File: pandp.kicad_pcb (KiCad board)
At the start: 2 copper layers, 95 x 89 mm, 93 parts, among them IC1 ADP2303-5, P1 CONN_01X02, P10 CONN_01X04, P11 CONN_01X02, P12 CONN_02X04, P13 CONN_01X02, P14 CONN_01X04, P15 CONN_01X04, P16 CONN_01X03, P17 CONN_01X03, P18 CONN_01X03, P19 CONN_01X03, P2 CONN_01X03, P20 CONN_01X03, P21 CONN_01X03, P22 CONN_02X03, P23 CONN_02X03, P24 CONN_02X03, P25 CONN_02X03, P26 CONN_01X03, P27 CONN_01X03, P28 CONN_01X03, P29 CONN_01X03, P3 CONN_01X02, P30 CONN_01X04, P31 CONN_01X04, P32 CONN_01X04, P33 CONN_01X04, P4 CONN_01X03, P6 CONN_01X03, P7 CONN_01X03, P8 USB_OTG, P9 CONN_01X02, Q1 IRF540N, Q2 IRF540N, SW1 SW_PUSH, U1 AP1117D33, U2 STM32F103RC, Y1 Crystal_Small - 2101357 on el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, Y2 Crystal_Small - 2063972 on el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

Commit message: first autorouter - dont like
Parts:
- removed C11, C7: CP, SMD_Packages:SMD-1210_Pol
- removed REF96, REF97, REF98, REF99: MountingHole_2-5mm, Mounting_Holes:MountingHole_2-5mm
- added R24: R, Resistors_SMD:R_0402, F.Cu at (139.0, 112.5)
- added REF80: MountingHole_2-5mm, Mounting_Holes:MountingHole_2-5mm, F.Cu at (195.0, 65.0)
- added REF81: MountingHole_2-5mm, Mounting_Holes:MountingHole_2-5mm, F.Cu at (195.0, 114.0)
- added REF82: MountingHole_2-5mm, Mounting_Holes:MountingHole_2-5mm, F.Cu at (85.5, 65.0)
- added REF83: MountingHole_2-5mm, Mounting_Holes:MountingHole_2-5mm, F.Cu at (85.5, 114.0)
- moved P1 153.7 mm to (195.8, 102.2)
- moved P3 153.7 mm to (195.8, 106.2)
- moved P4 148.2 mm to (195.8, 87.5)
- moved P2 148.2 mm to (195.8, 91.2)
- moved D1 145.0 mm to (192.2, 96.0), turned to 0 degrees
- moved P6 135.9 mm to (183.1, 114.5), turned to 270 degrees
- moved C1 134.8 mm to (186.8, 89.2)
- moved C3 127.0 mm to (183.0, 89.3)
- moved R1 126.1 mm to (181.2, 84.5)
- moved Q1 123.9 mm to (180.0, 108.0), turned to 0 degrees
- moved R2 121.9 mm to (185.2, 102.5), turned to 0 degrees
- moved C8 119.5 mm to (179.0, 89.2), turned to 270 degrees
- moved P7 118.6 mm to (171.5, 114.5), turned to 270 degrees
- moved D2 118.1 mm to (182.3, 95.5), turned to 180 degrees
- moved IC1 116.3 mm to (173.2, 89.5)
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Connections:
- C12 pad 2: GND -> GNDD
- C13 pad 2: GND -> GNDD
- C4 pad 2: GND -> GNDD
- C6 pad 2: GND -> GNDD
- P8 pad 1: +5V -> +5VL
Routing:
- net GND: track 544.3 -> 467.5 mm, vias 2 -> 0
- net CONT_2: track 20.9 -> 93.5 mm, vias 0 -> 2
- net +5VL: track 0.00 -> 72.0 mm
- net CONT_1: track 24.6 -> 90.1 mm, vias 0 -> 1
- net +5V: track 163.4 -> 99.9 mm, vias 0 -> 1
- net GNDD: track 52.6 -> 112.2 mm, vias 3 -> 0
- net +3V3: track 470.3 -> 414.5 mm, vias 3 -> 6
- net DIR_B: track 70.1 -> 116.3 mm, vias 1 -> 0
- net END_A: track 51.8 -> 9.65 mm, vias 0 -> 1
- net STEP_B: track 57.9 -> 99.6 mm, vias 1 -> 0
- net SCL_1: track 50.6 -> 10.6 mm, vias 1 -> 0
- net SDA_2: track 62.3 -> 33.5 mm
- net END_Y: track 40.8 -> 12.5 mm
- net SCL_2: track 60.0 -> 32.6 mm
- net SDA_1: track 49.3 -> 22.0 mm, vias 1 -> 0
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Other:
- board outline removed
- net class 12v: trace_width 0.6 -> 1
- net class 5v: trace_width 0.4 -> 0.7

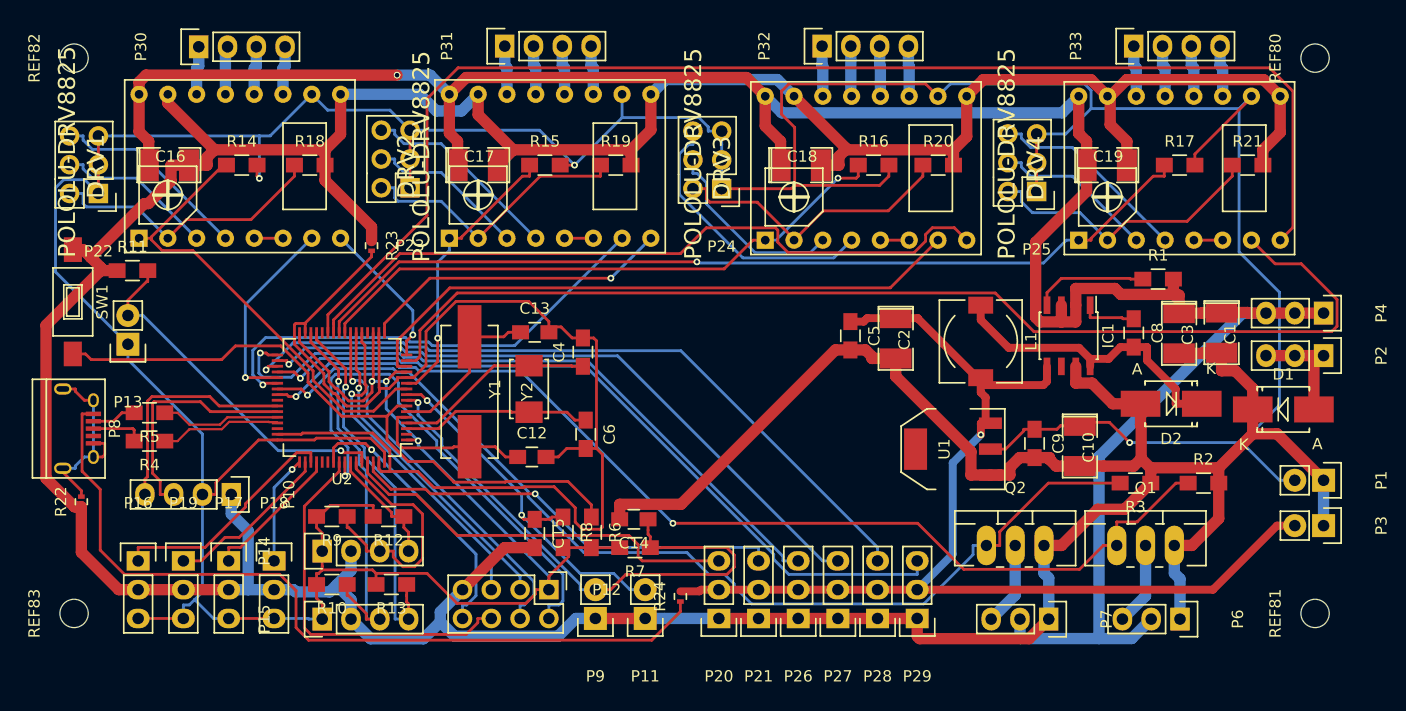
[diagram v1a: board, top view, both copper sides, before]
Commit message: power self-routed
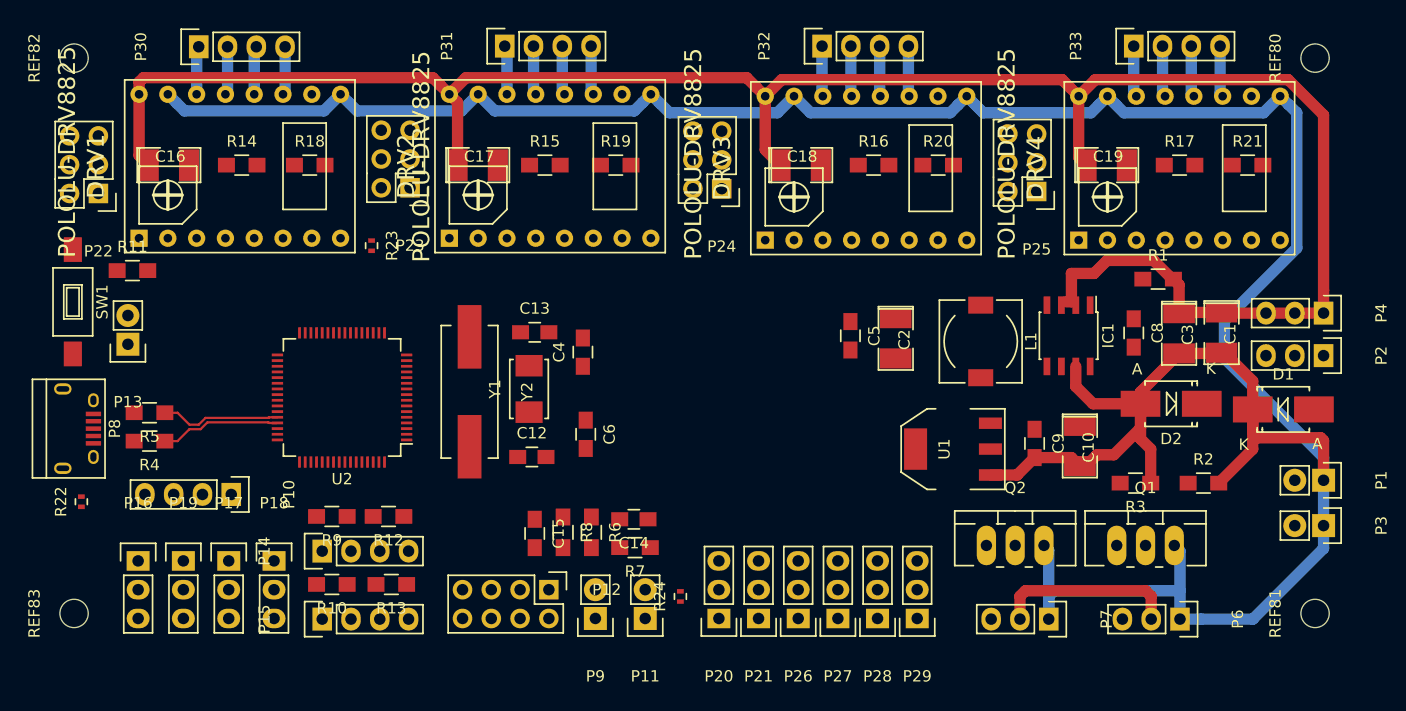
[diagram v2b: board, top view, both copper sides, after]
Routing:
- net +3V3: track 414.5 -> 0.00 mm, vias 6 -> 0
- net GND: track 467.5 -> 264.8 mm
- net DIR_B: track 116.3 -> 0.00 mm
- net GNDD: track 112.2 -> 0.00 mm
- net +5V: track 99.9 -> 0.00 mm, vias 1 -> 0
- net STEP_B: track 99.6 -> 0.00 mm
- net CONT_2: track 93.5 -> 0.00 mm, vias 2 -> 0
- net CONT_1: track 90.1 -> 0.00 mm, vias 1 -> 0
- net EN_B: track 80.3 -> 0.00 mm, vias 1 -> 0
- net +5VL: track 72.0 -> 0.00 mm
- net SERV_6: track 66.7 -> 0.00 mm, vias 1 -> 0
- net SERV_5: track 64.8 -> 0.00 mm, vias 1 -> 0
- net DIR_A: track 63.6 -> 0.00 mm
- net SERV_3: track 59.8 -> 0.00 mm, vias 1 -> 0
- net SERV_4: track 58.1 -> 0.00 mm, vias 1 -> 0
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
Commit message: pre-route-import
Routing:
- net GND: track 264.8 -> 341.3 mm
- net +12V: track 199.6 -> 183.6 mm
- net Net-(P6-Pad3): track 0.00 -> 7.40 mm
- net Net-(P7-Pad3): track 0.00 -> 7.38 mm
- net Net-(P8-Pad3): track 0.00 -> 4.05 mm
- net Net-(P8-Pad2): track 0.00 -> 3.91 mm
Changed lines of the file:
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@@
   (general
     (links 258)
-    (no_connects 258)
+    (no_connects 186)
     (area 79.7197 56.316416 219 138.700001)
     (thickness 1.6)
     (drawings 6)
-    (tracks 169)
+    (tracks 199)
     (zones 0)
     (modules 92)
@@
   (gr_line (start 82.5 60.75) (end 82.5 122.5) (layer Cmts.User) (width 0.2))
   (gr_line (start 200 62) (end 80 62) (layer Cmts.User) (width 0.2))
+  (segment (start 119.775 111.903) (end 118.553686 111.903) (width 1) (layer B.Cu) (net 1))
+  (segment (start 118.553686 111.903) (end 109.354 111.903) (width 1) (layer B.Cu) (net 1))
+  (segment (start 109.935 108.5) (end 109.935 110.516) (width 1) (layer B.Cu) (net 1))
+  (segment (start 109.935 110.516) (end 109.935 112.484) (width 1) (layer B.Cu) (net 1))
+  (segment (start 103.145 111.903) (end 109.354 111.903) (width 1) (layer B.Cu) (net 1))
+  (segment (start 109.354 111.903) (end 109.935 112.484) (width 1) (layer B.Cu) (net 1))
+  (segment (start 109.935 112.484) (end 109.935 114.5) (width 1) (layer B.Cu) (net 1))
+  (segment (start 99.1447 111.903) (end 103.145 111.903) (width 1) (layer B.Cu) (net 1))
+  (segment (start 95.1447 111.903) (end 99.1447 111.903) (width 1) (layer B.Cu) (net 1))
+  (segment (start 91.1547 111.903) (end 95.1447 111.903) (width 1) (layer B.Cu) (net 1))
+  (segment (start 149.395 114.443) (end 152.895 114.443) (width 1) (layer B.Cu) (net 1))
+  (segment (start 145.895 114.443) (end 149.395 114.443) (width 1) (layer B.Cu) (net 1))
+  (segment (start 142.395 114.443) (end 145.895 114.443) (width 1) (layer B.Cu) (net 1))
+  (segment (start 135.895 114.443) (end 142.395 114.443) (width 1) (layer B.Cu) (net 1))
+  (segment (start 131.5 114.443) (end 135.895 114.443) (width 1) (layer B.Cu) (net 1))
+  (segment (start 156.395 114.443) (end 152.895 114.443) (width 1) (layer B.Cu) (net 1))
+  (segment (start 159.895 114.443) (end 156.395 114.443) (width 1) (layer B.Cu) (net 1))
+  (segment (start 171.5 114.5) (end 171.5 112.03) (width 1) (layer B.Cu) (net 1))
+  (segment (start 171.5 112.03) (end 171.5 108.42) (width 1) (layer B.Cu) (net 1))
+  (segment (start 159.895 114.443) (end 161.911 114.443) (width 1) (layer B.Cu) (net 1))
+  (segment (start 161.911 114.443) (end 164.324 112.03) (width 1) (layer B.Cu) (net 1))
+  (segment (start 164.324 112.03) (end 171.5 112.03) (width 1) (layer B.Cu) (net 1))
   (segment (start 109.015 68.1927) (end 107.552999 69.654701) (width 1) (layer B.Cu) (net 1))
   (segment (start 94.536999 68.954699) (end 93.775 68.1927) (width 1) (layer B.Cu) (net 1))
@@
   (segment (start 171.5 112.484) (end 171.984 112) (width 1) (layer B.Cu) (net 1))
   (segment (start 171.984 112) (end 183.08 112) (width 1) (layer B.Cu) (net 1))
-  (segment (start 171.5 114.5) (end 171.5 108.42) (width 1) (layer B.Cu) (net 1))
   (segment (start 171.5 108.42) (end 171.08 108) (width 1) (layer B.Cu) (net 1))
   (segment (start 183.08 108.5) (end 182.58 108) (width 1) (layer B.Cu) (net 1))
@@
   (segment (start 184.9436 114.5) (end 183.08 114.5) (width 1) (layer B.Cu) (net 1))
   (segment (start 195.75 106.25) (end 195.75 102.25) (width 1) (layer B.Cu) (net 1))
-  (segment (start 168.96 114.5) (end 168.96 112.484) (width 1) (layer F.Cu) (net 12))
-  (segment (start 180.54 112.484) (end 180.54 114.5) (width 1) (layer F.Cu) (net 12))
-  (segment (start 168.96 112.484) (end 169.444 112) (width 1) (layer F.Cu) (net 12))
-  (segment (start 169.444 112) (end 180.056 112) (width 1) (layer F.Cu) (net 12))
-  (segment (start 180.056 112) (end 180.54 112.484) (width 1) (layer F.Cu) (net 12))
   (segment (start 173.5 86.5) (end 173 86.5) (width 1) (layer F.Cu) (net 12))
   (segment (start 173.5 84) (end 173.5 86.5) (width 1) (layer F.Cu) (net 12))
@@
   (segment (start 179 63.9427) (end 179 68.1377) (width 1) (layer B.Cu) (net 56))
   (segment (start 179 68.1377) (end 179.225 68.3627) (width 1) (layer B.Cu) (net 56))
+  (segment (start 177.93 111.01043) (end 178 111.08043) (width 1) (layer F.Cu) (net 58))
+  (segment (start 178 111.08043) (end 178 114.5) (width 1) (layer F.Cu) (net 58))
+  (segment (start 180.04 108) (end 180.04 108.90043) (width 1) (layer F.Cu) (net 58))
+  (segment (start 180.04 108.90043) (end 177.93 111.01043) (width 1) (layer F.Cu) (net 58))
+  (segment (start 168.54 108) (end 168.54 108.90043) (width 1) (layer F.Cu) (net 59))
+  (segment (start 166.42 112.484) (end 166.42 114.5) (width 1) (layer F.Cu) (net 59))
+  (segment (start 168.54 108.90043) (end 166.42 111.02043) (width 1) (layer F.Cu) (net 59))
+  (segment (start 166.42 111.02043) (end 166.42 112.484) (width 1) (layer F.Cu) (net 59))
+  (segment (start 88.5479 97.0421) (end 89.2973 96.2927) (width 0.25) (layer F.Cu) (net 60))
+  (segment (start 89.2973 96.2927) (end 90.8047 96.2927) (width 0.25) (layer F.Cu) (net 60))
+  (segment (start 87.20724 97.0421) (end 88.5479 97.0421) (width 0.25) (layer F.Cu) (net 60))
+  (segment (start 88.5679 97.6921) (end 89.6688 98.793) (width 0.25) (layer F.Cu) (net 61))
+  (segment (start 89.6688 98.793) (end 90.8047 98.793) (width 0.25) (layer F.Cu) (net 61))
+  (segment (start 87.20724 97.6921) (end 88.5679 97.6921) (width 0.25) (layer F.Cu) (net 61))
   (segment (start 97.265834 97.1427) (end 102.645 97.1427) (width 0.2) (layer F.Cu) (net 88))
   (segment (start 93.5047 98.793) (end 94.6297 98.793) (width 0.2) (layer F.Cu) (net 88))

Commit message: final - V1
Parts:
- moved REF80 0.56 mm to (195.5, 64.8)
- moved REF81 0.56 mm to (195.5, 114.2)
- moved REF82 0.25 mm to (85.5, 64.8)
- moved REF83 0.25 mm to (85.5, 114.2)
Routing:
- net +3V3: track 0.00 -> 425.2 mm, vias 0 -> 3
- net GND: track 341.3 -> 519.7 mm
- net +5V: track 0.00 -> 93.8 mm
- net CONT_2: track 0.00 -> 93.4 mm, vias 0 -> 2
- net GNDD: track 0.00 -> 92.9 mm
- net DIR_B: track 0.00 -> 91.6 mm, vias 0 -> 1
- net CONT_1: track 0.00 -> 85.7 mm, vias 0 -> 2
- net STEP_B: track 0.00 -> 80.7 mm, vias 0 -> 1
- net EN_B: track 0.00 -> 80.2 mm
- net +5VL: track 0.00 -> 78.4 mm
- net Net-(C8-Pad2): track 0.00 -> 70.1 mm
- net SERV_6: track 0.00 -> 67.4 mm, vias 0 -> 1
- net SERV_5: track 0.00 -> 63.5 mm, vias 0 -> 1
- net MEASURE_1: track 0.00 -> 61.1 mm, vias 0 -> 1
- net +12V: track 183.6 -> 243.9 mm
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- added copper zone on F.Cu, net +12V
- added copper zone on B.Cu, net GND
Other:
- board outline added: 116 x 55.5 mm
- board text added: "+"
- board text added: "+3.3V"
- board text added: "+5V"
- board text added: "-"
- board text added: "1"
- board text added: "12V IN"
- board text added: "2"
- board text added: "A"
- board text added: "B"
- board text added: "BOOT0"
- board text added: "D1"
- board text added: "D2"
- board text added: "D3"
- board text added: "G"
- board text added: "I2C"
- board text added: "M0"
- board text added: "M1"
- board text added: "MI"
- board text added: "MO"
- board text added: "P"
- board text added: "PaPaPaR - v1 - Takigama me@pjr.cc"
- board text added: "RX"
- board text added: "S"
- board text added: "SCK"
- board text added: "SCL"
- board text added: "SDA"
- board text added: "SPI"
- board text added: "STOPS"
- board text added: "Servo"
- board text added: "TX"
- board text added: "UART"
- board text added: "X"
- board text added: "Y"
- board text added: "uS"
